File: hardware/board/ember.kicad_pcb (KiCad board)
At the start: 4 copper layers, 150 x 50 mm, 134 parts, among them Q2 2SC1815_C727146, Q3 IRF1018ESTRLPBF, SW1 EC11E18244A5, SW2 SW_Push, SW3 SW_Push, U1 TPS25730D, U10 NT3H2111W0FHKH, U11 DB128L-5.08-2P-BK-S, U12 MAX31865xTP, U13 MAX6675ISA+T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

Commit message: udpate pcb with fixes
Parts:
- removed Q3: IRF1018ESTRLPBF, lcsc:TO-263-3_L10.2-W10.7-P5.08-LS16.2-BR
- removed R21: 1K, Resistor_SMD:R_0402_1005Metric
- removed U7: TLP183(GRH-TPL,E(T, lcsc:SOIC-4_L3.6-W4.4-P2.54-LS7.0-TL
- added C46: 4.7uF, Capacitor_SMD:C_0603_1608Metric, F.Cu at (151.7, 76.7)
- added C47: 100nF, Capacitor_SMD:C_0603_1608Metric, F.Cu at (150.1, 76.7)
- added H4: MountingHole, MountingHole:MountingHole_2.2mm_M2, F.Cu at (128.5, 73.9)
- added Q1: IRFS7440TRLPBF, lcsc:TO-263-2_L10.0-W9.1-P5.08-LS15.2-BR, F.Cu at (137.3, 78.6)
- added U2: TC4431EOA, lcsc:SOIC-8_L4.9-W3.9-P1.27-LS6.0-BL, F.Cu at (150.9, 72.4)
- moved D3 3.14 mm to (145.2, 73.7)
- moved R22 2.59 mm to (143.4, 73.0)
- moved D13 2.41 mm to (126.5, 106.4), turned to 180 degrees
- moved R24 1.92 mm to (156.4, 72.5)
- moved H3 0.99 mm to (128.5, 111.1)
- moved H2 0.56 mm to (206.9, 67.0)
- moved H1 0.09 mm to (206.9, 111.1)
- renumbered SWDIO to TP1, SWCLK to TP2, GND to TP3
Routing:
- net PPHV: track 10.8 -> 28.2 mm, vias 191 -> 192
- net Net-(U7-COL): track 6.23 -> 0.00 mm
- net +3.3V: track 71.4 -> 76.4 mm, vias 66 -> 67
- net Net-(D3-K): track 14.0 -> 10.7 mm
- net /HEATBED: track 75.3 -> 73.3 mm
- net /I2C_SCL: track 148.8 -> 150.2 mm
- net /I2C_SDA: track 150.3 -> 151.8 mm
- net Net-(D5-A): track 0.00 -> 1.20 mm
- net Net-(D7-A): track 0.00 -> 1.19 mm
- net Net-(D6-A): track 0.00 -> 1.19 mm
- net Net-(U2-IN): track 1.88 -> 2.80 mm
- net Net-(D2-A): track 45.2 -> 44.6 mm
- net GND: track 24.4 -> 24.6 mm, vias 1180 -> 784
- removed copper zone on In1.Cu, net PPHV
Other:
- board text added: "GND"
- board text added: "SWCLK"
- board text added: "SWDIO"

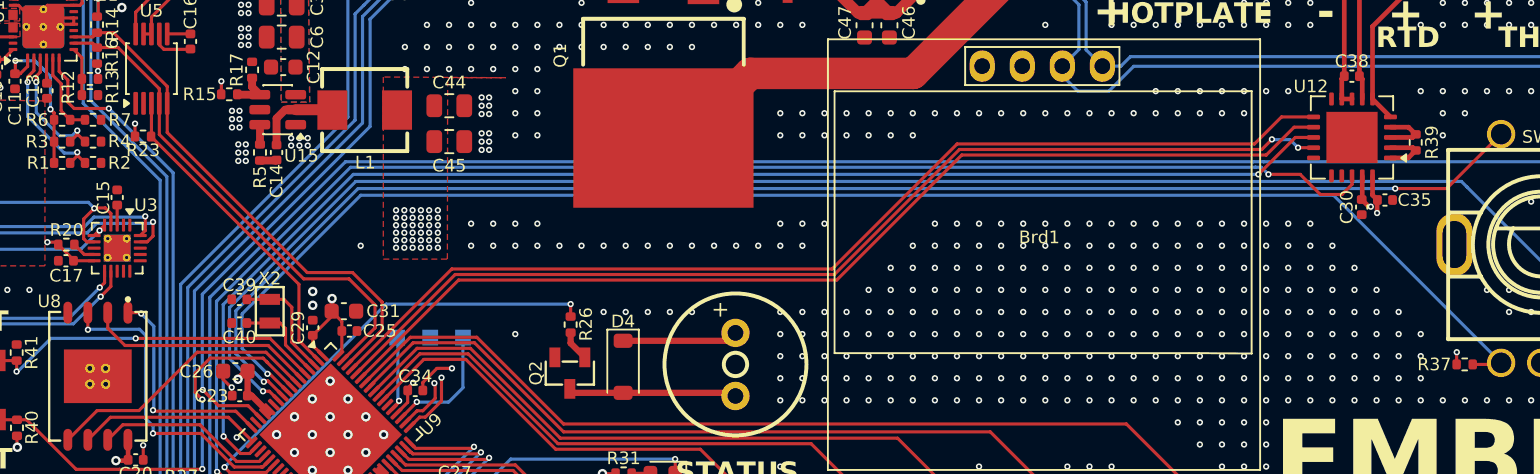
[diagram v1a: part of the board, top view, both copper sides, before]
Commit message: finish board and prod/case files
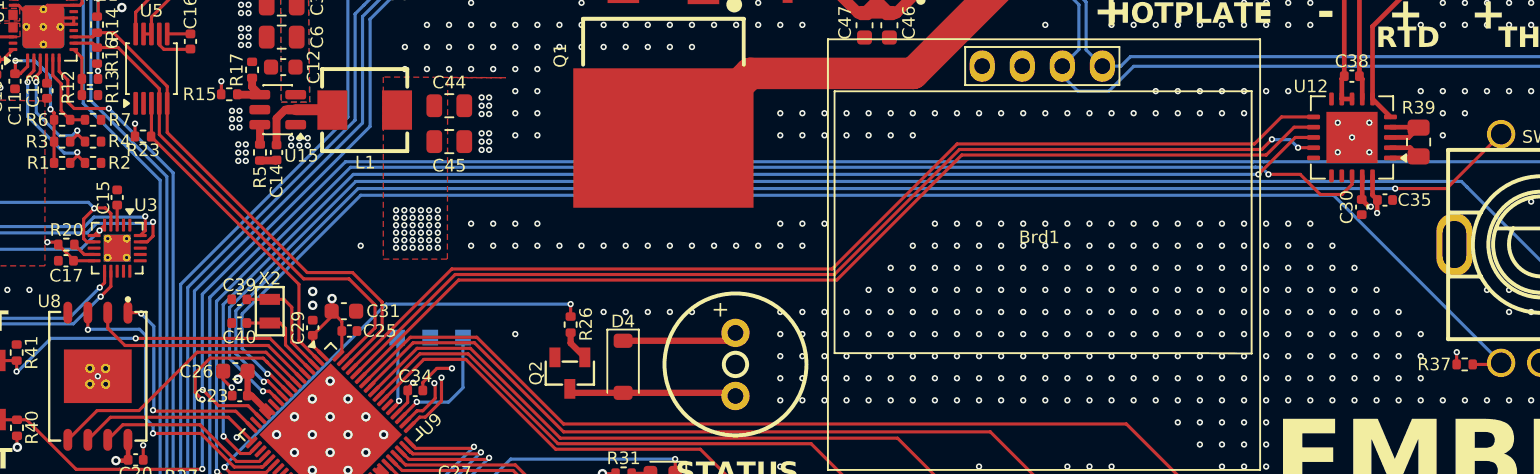
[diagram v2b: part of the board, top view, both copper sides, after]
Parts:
- R39: footprint Resistor_SMD:R_0402_1005Metric -> Resistor_SMD:R_0805_2012Metric
- moved R39 0.18 mm to (185.2, 84.0)
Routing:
- net GND: vias 784 -> 790

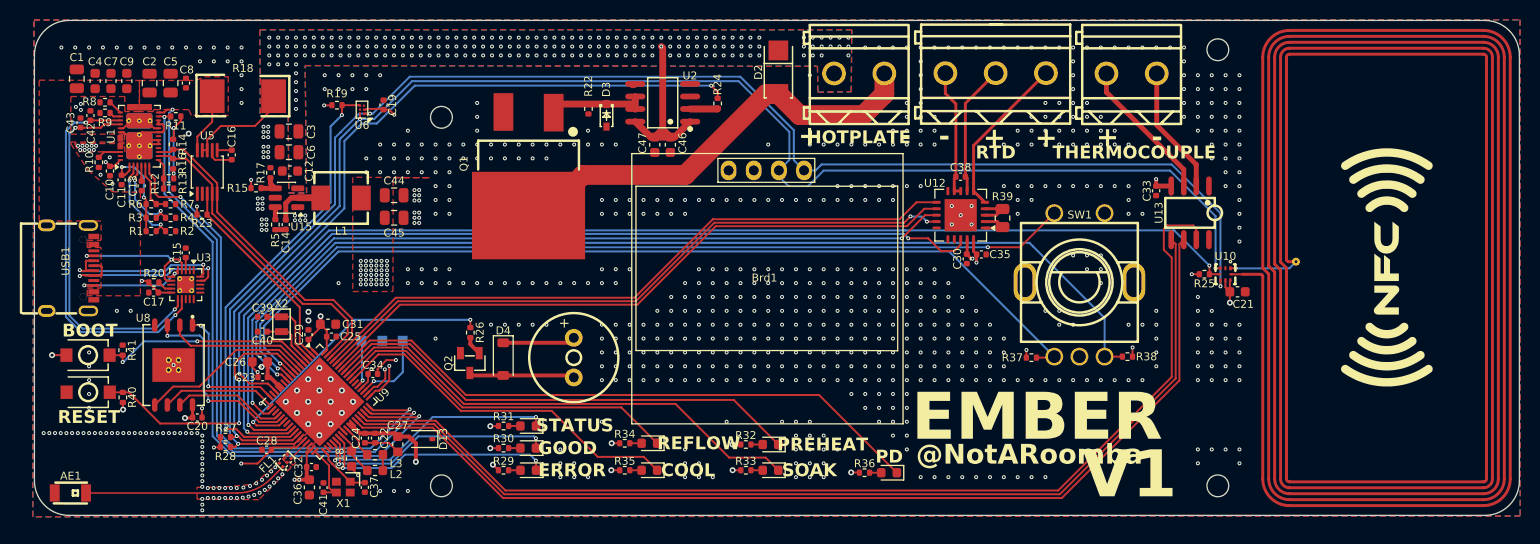
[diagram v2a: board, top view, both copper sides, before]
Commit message: fixed via sizing
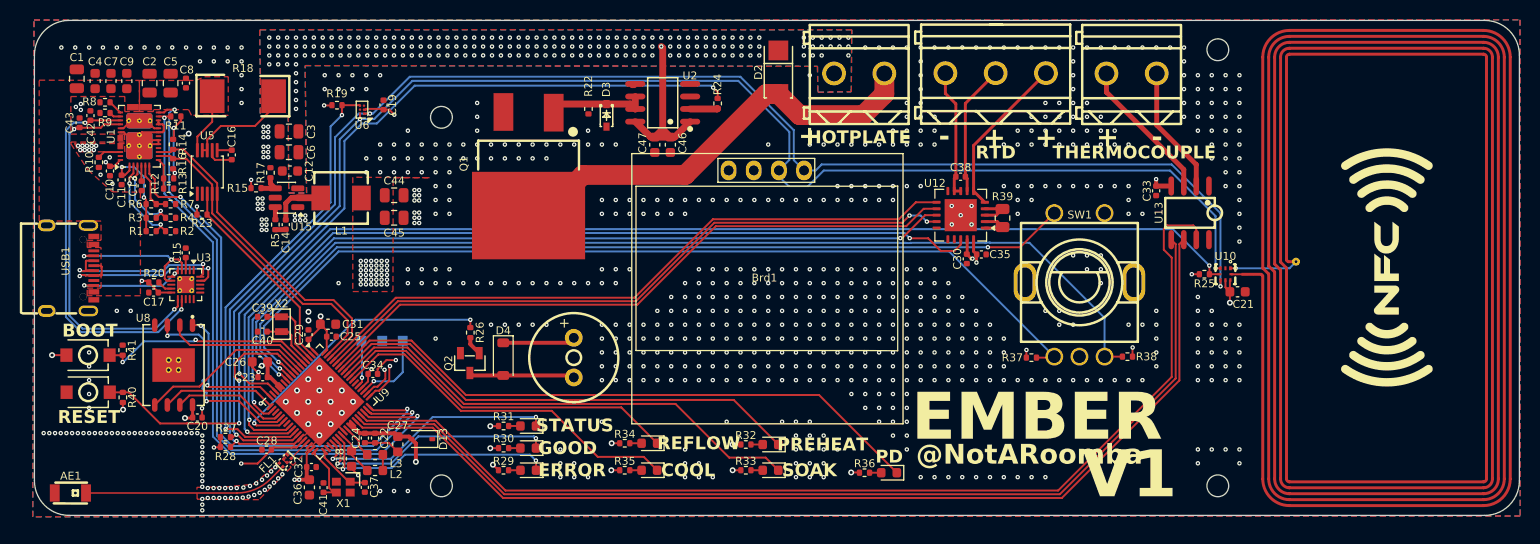
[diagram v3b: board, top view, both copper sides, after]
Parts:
- moved C43 0.09 mm to (92.0, 74.4)
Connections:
- U8 pad : (no net) -> GND
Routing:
- net /DP: track 47.2 -> 46.0 mm
- net LDO_3V3: track 35.8 -> 35.1 mm
- net /C_CC1: track 14.3 -> 14.9 mm
- net GND: track 24.6 -> 24.8 mm, vias 790 -> 789
